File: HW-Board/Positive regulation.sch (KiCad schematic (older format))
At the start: 16 parts, among them Q2 Si4435, U2 MCP4725, U3 AD5245, U4 OP07, U5 INA219POS

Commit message: sync
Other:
- note added: "LM395 ?"
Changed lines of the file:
@@
 	1    0    0    -1
 $EndComp
+Text Notes 6350 2200 0    50   ~ 0
+LM395  ?
 $EndSCHEMATC

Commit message: SYNC
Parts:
- Q2: symbol Peters:Si4435 -> BreadbaordPSU-rescue:Si4435-Peters
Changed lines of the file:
@@
 VposOut
 $Comp
-L Peters:Si4435 Q?
+L BreadbaordPSU-rescue:Si4435-Peters Q?
 U 1 1 5CFA01F0
 P 6400 2650
 AR Path="/5CFAD453/5CFA01F0" Ref="Q?"  Part="1"
 AR Path="/5CF8F081/5CFA01F0" Ref="Q2"  Part="1"
+AR Path="/5CFA01F0" Ref="Q2"  Part="1"
 F 0 "Q2" V 6743 2650 50  0000 C CNN
 F 1 "Si4435" V 6652 2650 50  0000 C CNN

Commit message: sync
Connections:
- net at C10.1, C11.1, C12.1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: no longer Q2.6 (D), Q2.7 (D), Q2.8 (D)
- new net: Q2.6 (D), Q2.7 (D), Q2.8 (D)
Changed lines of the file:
@@
 	1    0    0    -1
 $EndComp
-Wire Wire Line
-	6750 2550 6600 2550
 Connection ~ 6750 2550
-Connection ~ 6600 2550
-Wire Wire Line
-	6600 2550 6550 2550
 $Comp
 L power:+12V #PWR?
 U 1 1 5CFA0200
-P 5900 2500
+P 5950 2500
 AR Path="/5CFA0200" Ref="#PWR?"  Part="1"
 AR Path="/5CFAD453/5CFA0200" Ref="#PWR?"  Part="1"
 AR Path="/5CF8F081/5CFA0200" Ref="#PWR0127"  Part="1"
-F 0 "#PWR0127" H 5900 2350 50  0001 C CNN
-F 1 "+12V" H 5915 2673 50  0000 C CNN
-F 2 "" H 5900 2500 50  0001 C CNN
-F 3 "" H 5900 2500 50  0001 C CNN
-	1    5900 2500
+F 0 "#PWR0127" H 5950 2350 50  0001 C CNN
+F 1 "+12V" H 5965 2673 50  0000 C CNN
+F 2 "" H 5950 2500 50  0001 C CNN
+F 3 "" H 5950 2500 50  0001 C CNN
+	1    5950 2500
 	1    0    0    -1
 $EndComp
@@
 	6250 2550 6200 2550
 Wire Wire Line
-	5900 2550 5900 2500
+	5950 2550 5950 2500
 Connection ~ 6200 2550
 Wire Wire Line
@@
 I2C_SCL
 Connection ~ 5950 2550
-Wire Wire Line
-	5950 2550 5900 2550
 $Comp
 L Device:C C?
@@
 Text Notes 6350 2200 0    50   ~ 0
 LM395  ?
+Wire Wire Line
+	6550 2550 6750 2550
 $EndSCHEMATC

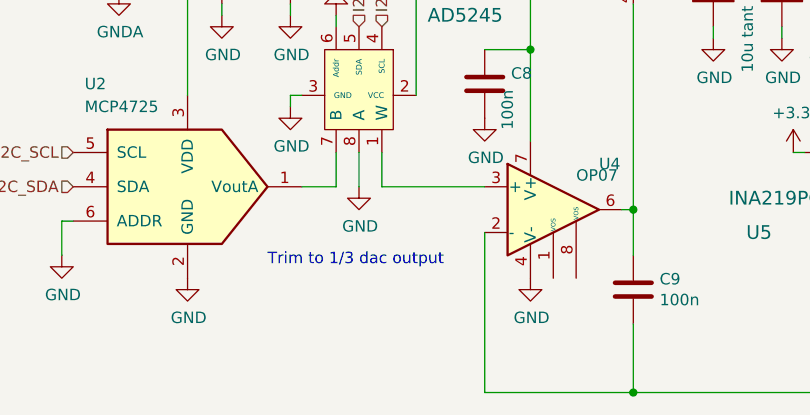
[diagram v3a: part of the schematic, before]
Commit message: 5v isolation and better opamps
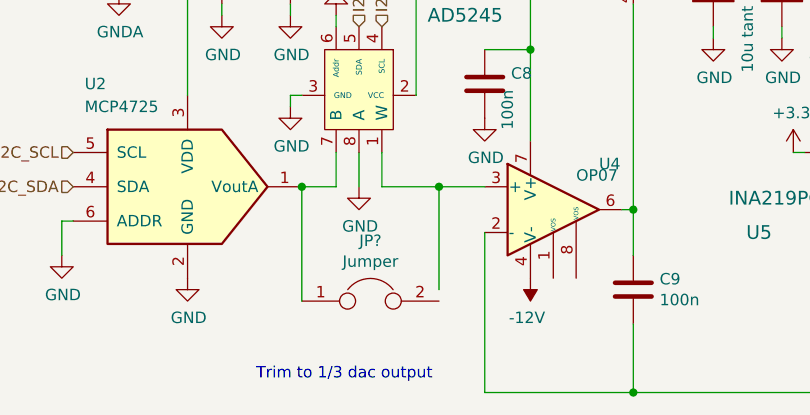
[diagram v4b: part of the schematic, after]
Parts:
- added JP?: Jumper, symbol Device:Jumper
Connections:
- net GND: no longer U4.4 (V-)
- net at U2.1 (VoutA), U3.7 (B): now also JP?.1
- new net -12V: U4.4 (V-)

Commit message: sync
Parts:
- removed Q2: Si4435, Package_SO:SOIC-8_3.9x4.9mm_P1.27mm, symbol BreadbaordPSU-rescue:Si4435-Peters
- added Q?: SI4466, Package_SO:SOIC-8_3.9x4.9mm_P1.27mm, symbol Peters:SI4466
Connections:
- net +12V: now also Q?.5 (D), Q?.6 (D), Q?.7 (D), Q?.8 (D)
- net at C10.1, C11.1, C12.1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: now also Q?.1 (S), Q?.2 (S), Q?.3 (S)
- net at C9.1, U4.6: now also Q?.4 (G)
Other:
- moved on the sheet: C9
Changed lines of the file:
@@
 	5950 2550 5950 2500
 Wire Wire Line
-	6400 3650 6350 3650
+	6450 3650 6350 3650
 Wire Wire Line
 	5750 3750 5750 4450
 Wire Wire Line
-	5750 4450 6400 4450
+	5750 4450 6450 4450
 Wire Wire Line
 	8450 4450 8450 2550
@@
 L Device:C C?
 U 1 1 5CFA023C
-P 6400 4000
+P 6450 4000
 AR Path="/5CFAD453/5CFA023C" Ref="C?"  Part="1"
 AR Path="/5CF8F081/5CFA023C" Ref="C9"  Part="1"
-F 0 "C9" H 6515 4046 50  0000 L CNN
-F 1 "100n" H 6515 3955 50  0000 L CNN
-F 2 "" H 6438 3850 50  0001 C CNN
-F 3 "~" H 6400 4000 50  0001 C CNN
-	1    6400 4000
-	1    0    0    -1
-$EndComp
-Wire Wire Line
-	6400 3850 6400 3650
-Connection ~ 6400 3650
-Wire Wire Line
-	6400 4150 6400 4450
+F 0 "C9" H 6565 4046 50  0000 L CNN
+F 1 "100n" H 6565 3955 50  0000 L CNN
+F 2 "" H 6488 3850 50  0001 C CNN
+F 3 "~" H 6450 4000 50  0001 C CNN
+	1    6450 4000
+	1    0    0    -1
+$EndComp
+Wire Wire Line
+	6450 3850 6450 3650
+Connection ~ 6450 3650
+Wire Wire Line
+	6450 4150 6450 4450
 Wire Wire Line
 	5950 2550 5950 2950
@@
 	3900 3700 3900 3850
 Wire Wire Line
-	6400 4450 8450 4450
-Connection ~ 6400 4450
+	6450 4450 8450 4450
+Connection ~ 6450 4450
 Wire Wire Line
 	7350 2550 7050 2550
@@
 LM395  ?
 Wire Wire Line
-	6400 2750 6400 3650
-Wire Wire Line
-	6550 2550 6750 2550
-Wire Wire Line
-	6200 2550 5950 2550
-Wire Wire Line
-	6250 2550 6200 2550
-Connection ~ 6200 2550
-$Comp
-L BreadbaordPSU-rescue:Si4435-Peters Q?
-U 1 1 5CFA01F0
-P 6400 2650
-AR Path="/5CFAD453/5CFA01F0" Ref="Q?"  Part="1"
-AR Path="/5CF8F081/5CFA01F0" Ref="Q2"  Part="1"
-AR Path="/5CFA01F0" Ref="Q2"  Part="1"
-F 0 "Q2" V 6743 2650 50  0000 C CNN
-F 1 "Si4435" V 6652 2650 50  0000 C CNN
-F 2 "Package_SO:SOIC-8_3.9x4.9mm_P1.27mm" H 6150 2950 50  0001 C CNN
-F 3 "https://www.vishay.com/docs/72123/72123.pdf" H 6250 3050 50  0001 C CNN
-	1    6400 2650
-	0    1    -1   0
-$EndComp
+	6450 2850 6450 3650
 $Comp
 L power:-12V #PWR?
@@
 Wire Wire Line
 	5550 3550 5750 3550
+$Comp
+L Peters:SI4466 Q?
+U 1 1 5D4F6E86
+P 6400 2650
+F 0 "Q?" V 6728 2650 50  0000 C CNN
+F 1 "SI4466" V 6637 2650 50  0000 C CNN
+F 2 "Package_SO:SOIC-8_3.9x4.9mm_P1.27mm" H 6250 2350 50  0001 C CNN
+F 3 "https://www.vishay.com/docs/71820/71820.pdf" H 6150 3000 50  0001 C CNN
+	1    6400 2650
+	0    -1   -1   0
+$EndComp
+Wire Wire Line
+	5950 2550 6200 2550
+Wire Wire Line
+	6600 2550 6750 2550
 $EndSCHEMATC

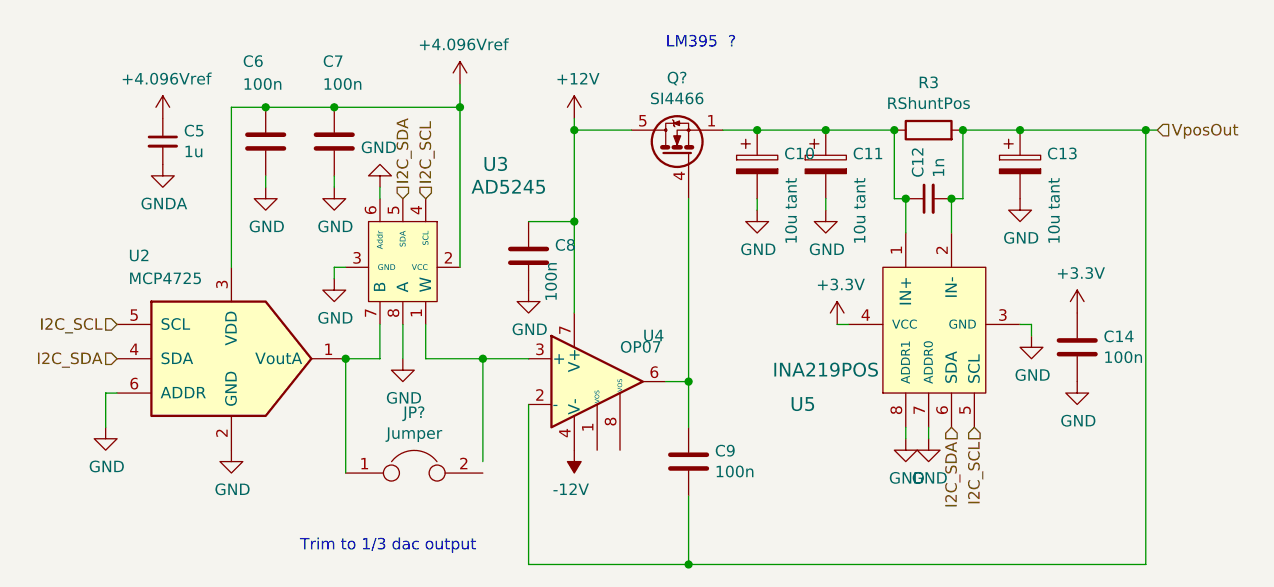
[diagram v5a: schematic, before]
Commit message: Boost converter added
Go go abvoe Vgs-th at maximum output
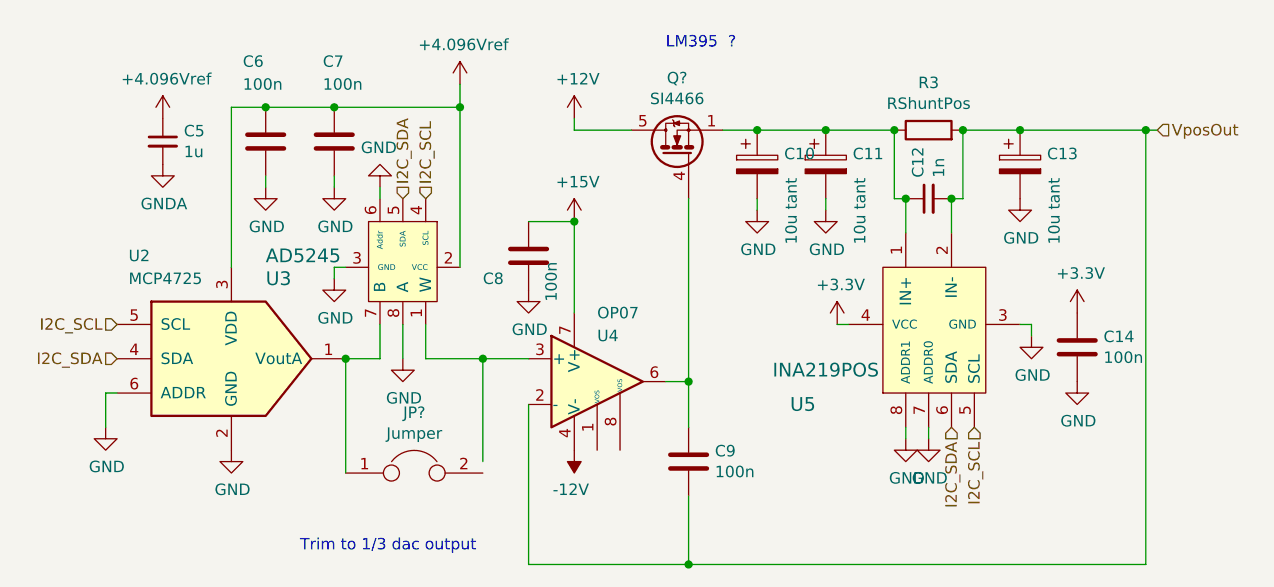
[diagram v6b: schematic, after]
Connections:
- net +12V: no longer C8.1, U4.7 (V+)
- new net +15V: C8.1, U4.7 (V+)
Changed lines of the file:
@@
 encoding utf-8
 Sheet 2 4
-Title ""
+Title "Isolated adjustible +/- VDC PSU"
 Date ""
 Rev ""
@@
 AR Path="/5CFAD453/5CFA01F6" Ref="U?"  Part="1"
 AR Path="/5CF8F081/5CFA01F6" Ref="U4"  Part="1"
-F 0 "U4" H 6250 3850 50  0000 L CNN
-F 1 "OP07" H 6150 3800 50  0000 L CNN
+F 0 "U4" H 6050 3850 50  0000 L CNN
+F 1 "OP07" H 6050 3950 50  0000 L CNN
 F 2 "" H 6100 3700 50  0001 C CNN
 F 3 "https://www.analog.com/media/en/technical-documentation/data-sheets/OP07.pdf" H 6100 3800 50  0001 C CNN
@@
 Text HLabel 3950 3400 0    50   Input ~ 0
 I2C_SCL
-Connection ~ 5950 2550
 $Comp
 L Device:C C?
@@
 AR Path="/5CFAD453/5CFA021D" Ref="C?"  Part="1"
 AR Path="/5CF8F081/5CFA021D" Ref="C8"  Part="1"
-F 0 "C8" H 5865 3146 50  0000 L CNN
+F 0 "C8" H 5550 3000 50  0000 L CNN
 F 1 "100n" V 5850 2900 50  0000 L CNN
 F 2 "" H 5788 2950 50  0001 C CNN
@@
 	6450 4150 6450 4450
 Wire Wire Line
-	5950 2550 5950 2950
-Wire Wire Line
 	5750 2950 5950 2950
-Connection ~ 5950 2950
 Wire Wire Line
 	5950 2950 5950 3350
@@
 AR Path="/5CFAD453/5CFA026A" Ref="U?"  Part="1"
 AR Path="/5CF8F081/5CFA026A" Ref="U3"  Part="1"
-F 0 "U3" V 4750 3500 60  0000 L CNN
-F 1 "AD5245" V 4850 3450 60  0000 L CNN
+F 0 "U3" V 5250 2550 60  0000 L CNN
+F 1 "AD5245" V 5150 2550 60  0000 L CNN
 F 2 "TO_SOT_Packages_SMD:SOT-23-8_Handsoldering" H 5050 3400 60  0001 C CNN
 F 3 "" H 5050 3400 60  0001 C CNN
@@
 Wire Wire Line
 	6600 2550 6750 2550
+$Comp
+L power:+15V #PWR?
+U 1 1 5D60B214
+P 5950 2950
+F 0 "#PWR?" H 5950 2800 50  0001 C CNN
+F 1 "+15V" H 5965 3123 50  0000 C CNN
+F 2 "" H 5950 2950 50  0001 C CNN
+F 3 "" H 5950 2950 50  0001 C CNN
+	1    5950 2950
+	1    0    0    -1
+$EndComp
+Connection ~ 5950 2950
 $EndSCHEMATC
